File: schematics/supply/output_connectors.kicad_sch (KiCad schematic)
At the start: 20 parts, among them J17 banana jack + fuse 20A, J18 Conn_02x04_Odd_Even, J19 banana jack + fuse 15A, J20 jst xh angle, J21 jst xh angle, Q10 IRLML0030, Q10 IRLML5203, U6 INA3221

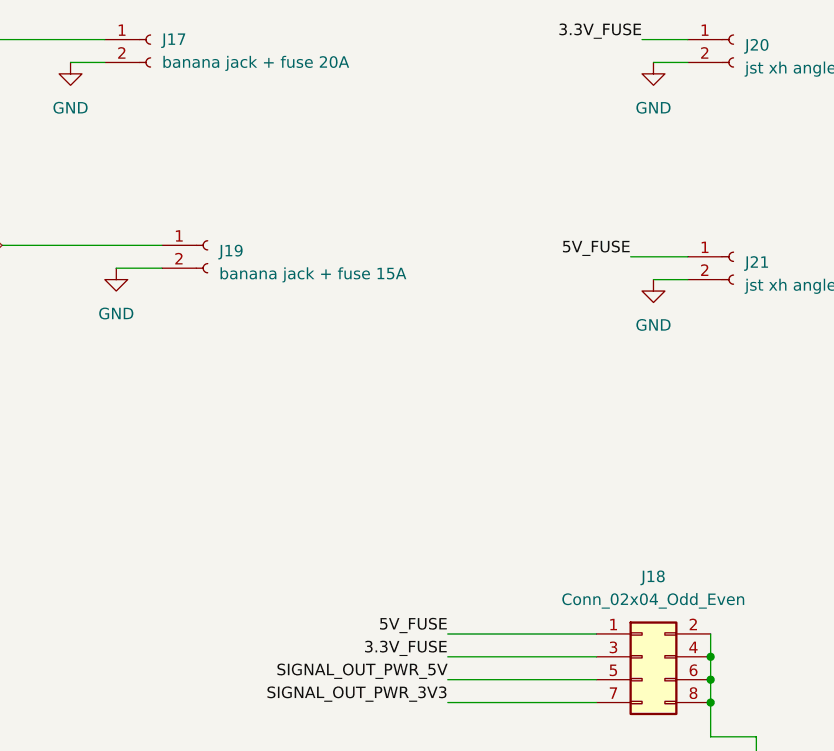
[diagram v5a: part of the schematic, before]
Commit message: Added over-voltage protection to 5V line
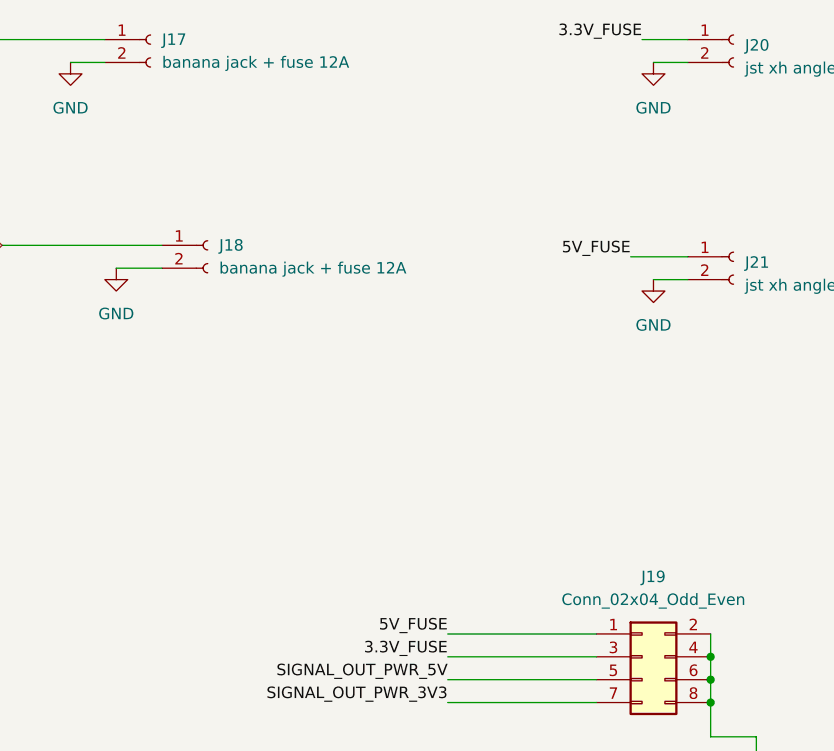
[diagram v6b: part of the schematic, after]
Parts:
- J17: value banana jack + fuse 20A -> banana jack + fuse 12A
- J18: renamed from J19; value banana jack + fuse 15A -> banana jack + fuse 12A
- renumbered J18 to J19
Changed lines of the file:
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@@
         )
         (path "/1e139717-fcd1-4008-a6ea-4c993845e928/39d9543b-2a42-4758-87e9-56ce3e85ea36"
-          (reference "#PWR099") (unit 1)
+          (reference "#PWR0103") (unit 1)
         )
       )
@@
         )
         (path "/1e139717-fcd1-4008-a6ea-4c993845e928/39d9543b-2a42-4758-87e9-56ce3e85ea36"
-          (reference "R76") (unit 1)
+          (reference "R78") (unit 1)
         )
       )
@@
         )
         (path "/1e139717-fcd1-4008-a6ea-4c993845e928/39d9543b-2a42-4758-87e9-56ce3e85ea36"
-          (reference "R78") (unit 1)
+          (reference "R77") (unit 1)
         )
       )
@@
       (effects (font (size 1.27 1.27)) (justify left))
     )
-    (property "Value" "banana jack + fuse 20A" (at 203.2 21.59 0)
+    (property "Value" "banana jack + fuse 12A" (at 203.2 21.59 0)
       (effects (font (size 1.27 1.27)) (justify left))
     )
@@
         )
         (path "/1e139717-fcd1-4008-a6ea-4c993845e928/39d9543b-2a42-4758-87e9-56ce3e85ea36"
-          (reference "#PWR094") (unit 1)
+          (reference "#PWR098") (unit 1)
         )
       )
@@
         )
         (path "/1e139717-fcd1-4008-a6ea-4c993845e928/39d9543b-2a42-4758-87e9-56ce3e85ea36"
-          (reference "R77") (unit 1)
+          (reference "R76") (unit 1)
         )
       )
@@
         )
         (path "/1e139717-fcd1-4008-a6ea-4c993845e928/39d9543b-2a42-4758-87e9-56ce3e85ea36"
-          (reference "#PWR090") (unit 1)
+          (reference "#PWR094") (unit 1)
         )
       )
@@
   (symbol (lib_id "Connector:Conn_01x02_Socket") (at 208.28 41.91 0) (unit 1)
     (in_bom yes) (on_board yes) (dnp no) (fields_autoplaced)
-    (property "Reference" "J19" (at 209.55 42.545 0)
-      (effects (font (size 1.27 1.27)) (justify left))
-    )
-    (property "Value" "banana jack + fuse 15A" (at 209.55 45.085 0)
+    (property "Reference" "J18" (at 209.55 41.91 0)
+      (effects (font (size 1.27 1.27)) (justify left))
+    )
+    (property "Value" "banana jack + fuse 12A" (at 209.55 44.45 0)
       (effects (font (size 1.27 1.27)) (justify left))
     )
@@
       (project "supply"
         (path "/1e139717-fcd1-4008-a6ea-4c993845e928/39d9543b-2a42-4758-87e9-56ce3e85ea36"
-          (reference "J19") (unit 1)
+          (reference "J18") (unit 1)
         )
       )
@@
         )
         (path "/1e139717-fcd1-4008-a6ea-4c993845e928/39d9543b-2a42-4758-87e9-56ce3e85ea36"
-          (reference "#PWR0101") (unit 1)
+          (reference "#PWR099") (unit 1)
         )
       )
@@
         )
         (path "/1e139717-fcd1-4008-a6ea-4c993845e928/39d9543b-2a42-4758-87e9-56ce3e85ea36"
-          (reference "#PWR097") (unit 1)
+          (reference "#PWR0104") (unit 1)
         )
       )
@@
         )
         (path "/1e139717-fcd1-4008-a6ea-4c993845e928/39d9543b-2a42-4758-87e9-56ce3e85ea36"
-          (reference "#PWR091") (unit 1)
+          (reference "#PWR095") (unit 1)
         )
       )
@@
         )
         (path "/1e139717-fcd1-4008-a6ea-4c993845e928/39d9543b-2a42-4758-87e9-56ce3e85ea36"
-          (reference "#PWR096") (unit 1)
+          (reference "#PWR0101") (unit 1)
         )
       )
@@
         )
         (path "/1e139717-fcd1-4008-a6ea-4c993845e928/39d9543b-2a42-4758-87e9-56ce3e85ea36"
-          (reference "#PWR093") (unit 1)
+          (reference "#PWR097") (unit 1)
         )
       )
@@
         )
         (path "/1e139717-fcd1-4008-a6ea-4c993845e928/39d9543b-2a42-4758-87e9-56ce3e85ea36"
-          (reference "#PWR095") (unit 1)
+          (reference "#PWR0100") (unit 1)
         )
       )
@@
   (symbol (lib_id "Connector_Generic:Conn_02x04_Odd_Even") (at 256.54 87.63 0) (unit 1)
     (in_bom yes) (on_board yes) (dnp no) (fields_autoplaced)
-    (property "Reference" "J18" (at 257.81 78.74 0)
+    (property "Reference" "J19" (at 257.81 78.74 0)
       (effects (font (size 1.27 1.27)))
     )
@@
       (project "supply"
         (path "/1e139717-fcd1-4008-a6ea-4c993845e928/39d9543b-2a42-4758-87e9-56ce3e85ea36"
-          (reference "J18") (unit 1)
+          (reference "J19") (unit 1)
         )
       )
@@
         )
         (path "/1e139717-fcd1-4008-a6ea-4c993845e928/39d9543b-2a42-4758-87e9-56ce3e85ea36"
-          (reference "#PWR098") (unit 1)
+          (reference "#PWR0102") (unit 1)
         )
       )
@@
         )
         (path "/1e139717-fcd1-4008-a6ea-4c993845e928/39d9543b-2a42-4758-87e9-56ce3e85ea36"
-          (reference "#PWR092") (unit 1)
-        )
-      )
+          (reference "#PWR096") (unit 1)
+        )
+      )

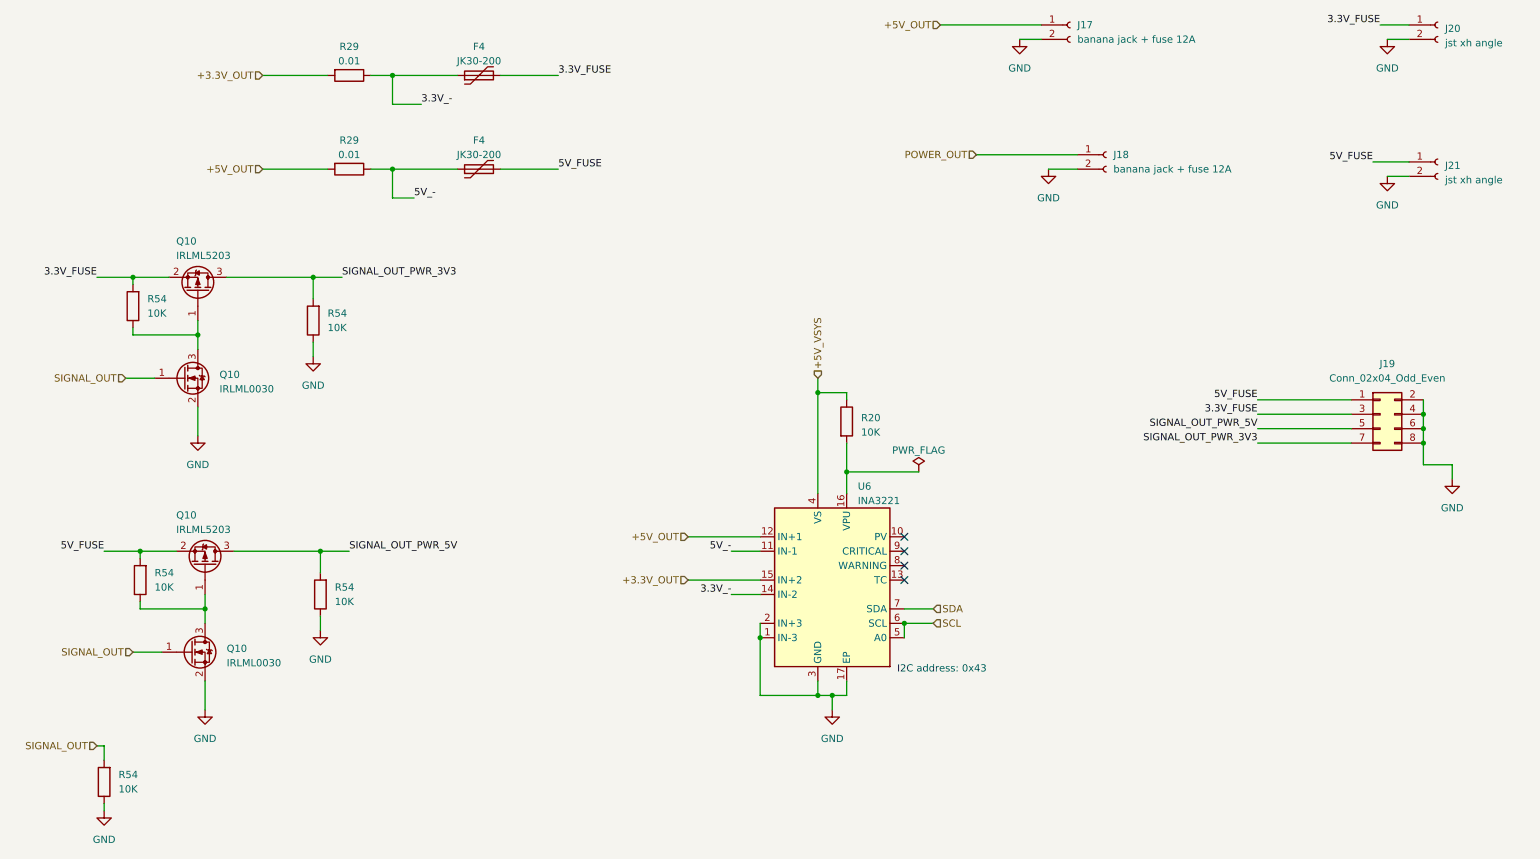
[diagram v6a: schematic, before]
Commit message: Fixed problem with 20V on one leg of comparator
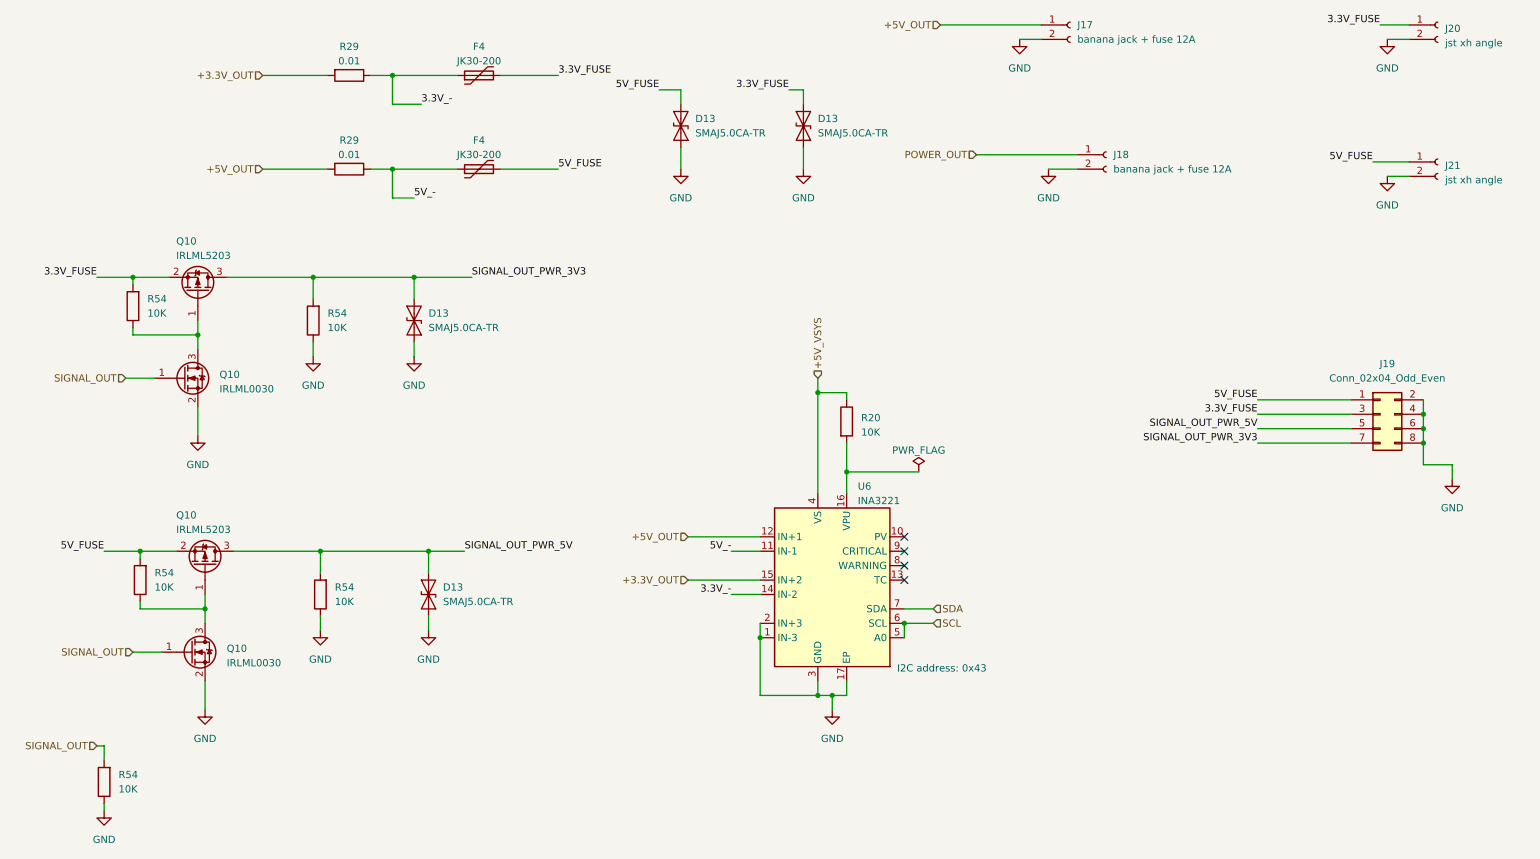
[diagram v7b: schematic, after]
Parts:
- added D13 (x4): SMAJ5.0CA-TR, Diode_SMD:D_SMA, symbol Diode:ESD9B3.3ST5G
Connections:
- net 3.3V_FUSE: now also D13.2 (A2)
- net 5V_FUSE: now also D13.2 (A2)
- net GND: now also D13.1 (A1), D13.1 (A1), D13.1 (A1), D13.1 (A1)
- net SIGNAL_OUT_PWR_3V3: now also D13.2 (A2)
- net SIGNAL_OUT_PWR_5V: now also D13.2 (A2)

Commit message: Some changes in board - Im preparing it to production
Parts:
- removed F4 (x2): JK30-200, Capacitor_THT:C_Disc_D11.0mm_W5.0mm_P5.00mm, symbol Device:Polyfuse
- added F2 (x2): 3A, Connector_Wire:SolderWire-0.75sqmm_1x02_P4.8mm_D1.25mm_OD2.3mm, symbol Device:Fuse
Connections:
- net 3.3V_-: now also F2.1
- net 3.3V_FUSE: now also J20.2 (Pin_2), F2.2; no longer J20.1 (Pin_1)
- net 5V_-: now also F2.1
- net 5V_FUSE: now also J21.2 (Pin_2), F2.2; no longer J21.1 (Pin_1)
- net GND: now also J20.1 (Pin_1), J21.1 (Pin_1); no longer J20.2 (Pin_2), J21.2 (Pin_2)
